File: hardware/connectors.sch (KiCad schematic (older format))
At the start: 16 parts, among them P1 Conn_01x12_Male, P10 Conn_01x12_Male, P11 Conn_01x12_Male, P12 Conn_01x12_Male, P13 Conn_01x12_Male, P14 Conn_01x12_Male, P15 Conn_01x12_Male, P16 Conn_01x12_Male, P2 Conn_01x12_Male, P3 Conn_01x12_Male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

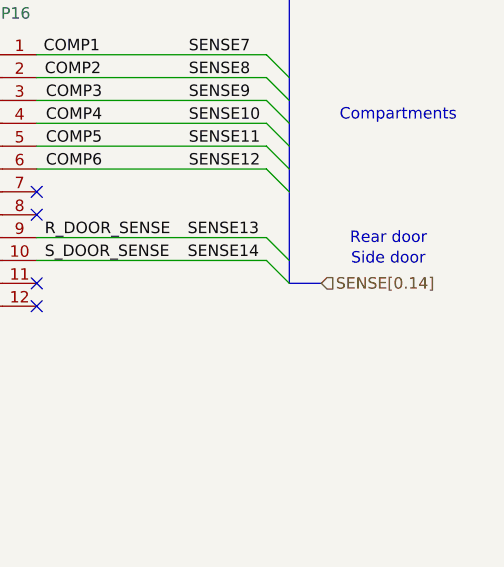
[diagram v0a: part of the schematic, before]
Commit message: hardware: fix mislabeled bus
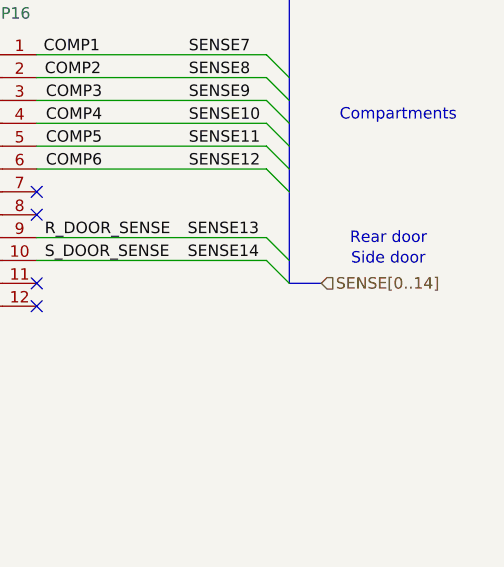
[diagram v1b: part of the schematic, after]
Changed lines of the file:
@@
 	14535 6650 14675 6650
 Text HLabel 14675 6650 2    50   Input ~ 0
-SENSE[0.14]
+SENSE[0..14]
 Wire Wire Line
 	13430 5950 14435 5950

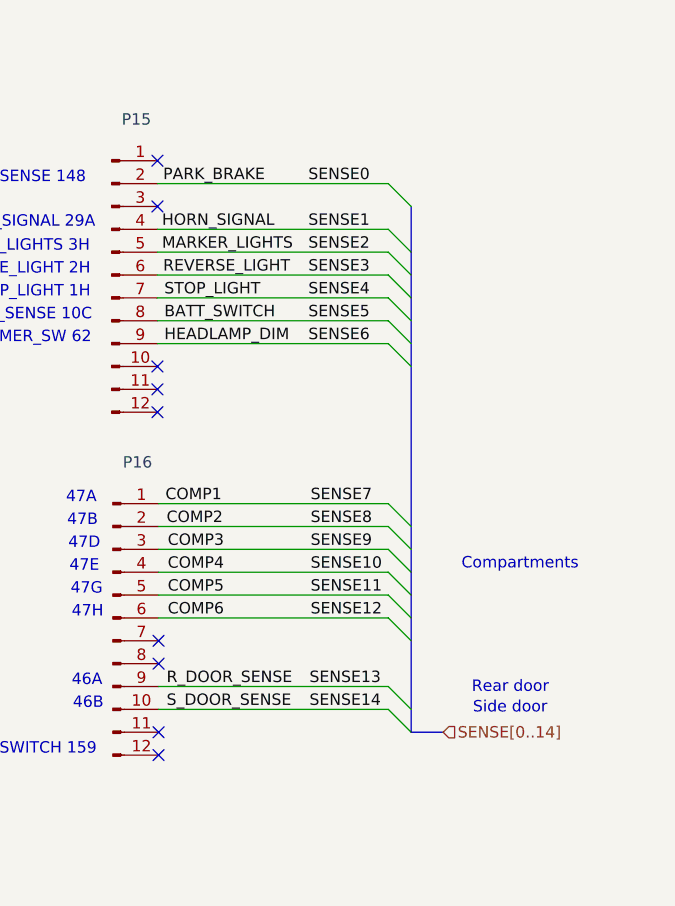
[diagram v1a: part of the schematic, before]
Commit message: hardware: split house and truck sense
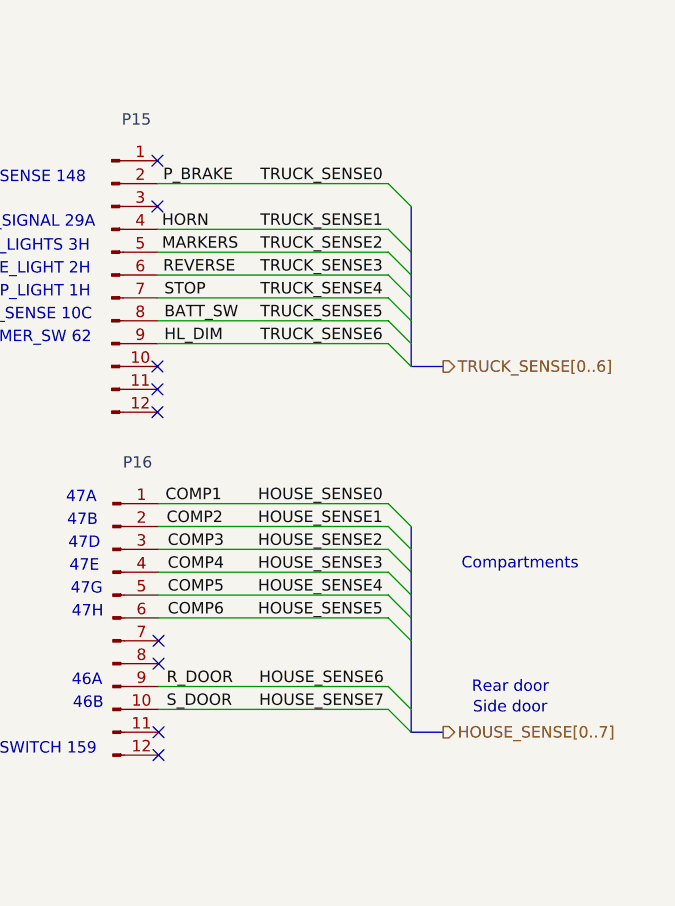
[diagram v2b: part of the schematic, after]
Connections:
- net BATT_SWITCH renamed BATT_SW
- net HEADLAMP_DIM renamed HL_DIM
- net HORN_SIGNAL renamed HORN
- net MARKER_LIGHTS renamed MARKERS
- net PARK_BRAKE renamed P_BRAKE
- net REVERSE_LIGHT renamed REVERSE
- net R_DOOR_SENSE renamed HOUSE_SENSE6
- net SENSE14 renamed HOUSE_SENSE7
- net SENSE4 renamed STOP
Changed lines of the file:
@@
 COMP6
 Text Label 13465 6450 0    50   ~ 0
-R_DOOR_SENSE
+R_DOOR
 Text Label 13465 6550 0    50   ~ 0
-S_DOOR_SENSE
-Text Label 14095 5650 0    50   ~ 0
-SENSE7
-Text Label 14095 5750 0    50   ~ 0
-SENSE8
-Text Label 14095 5850 0    50   ~ 0
-SENSE9
-Text Label 14095 5950 0    50   ~ 0
-SENSE10
-Text Label 14095 6050 0    50   ~ 0
-SENSE11
-Text Label 14095 6150 0    50   ~ 0
-SENSE12
-Text Label 14090 6450 0    50   ~ 0
-SENSE13
-Text Label 14090 6550 0    50   ~ 0
-SENSE14
+S_DOOR
+Text Label 13865 5650 0    50   ~ 0
+HOUSE_SENSE0
+Text Label 13865 5750 0    50   ~ 0
+HOUSE_SENSE1
+Text Label 13865 5850 0    50   ~ 0
+HOUSE_SENSE2
+Text Label 13865 5950 0    50   ~ 0
+HOUSE_SENSE3
+Text Label 13865 6050 0    50   ~ 0
+HOUSE_SENSE4
+Text Label 13865 6150 0    50   ~ 0
+HOUSE_SENSE5
+Text Label 13870 6450 0    50   ~ 0
+HOUSE_SENSE6
+Text Label 13870 6550 0    50   ~ 0
+HOUSE_SENSE7
 Text Label 13450 4250 0    50   ~ 0
-PARK_BRAKE
+P_BRAKE
 NoConn ~ 13425 4350
 Text Label 13445 4450 0    50   ~ 0
-HORN_SIGNAL
+HORN
 Text Label 13445 4550 0    50   ~ 0
-MARKER_LIGHTS
+MARKERS
 Text Label 13450 4650 0    50   ~ 0
-REVERSE_LIGHT
+REVERSE
 Text Label 13455 4750 0    50   ~ 0
-STOP_LIGHT
+STOP
 Text Label 13455 4850 0    50   ~ 0
-BATT_SWITCH
+BATT_SW
 Text Label 13455 4950 0    50   ~ 0
-HEADLAMP_DIM
-Text Label 14085 4950 0    50   ~ 0
-SENSE6
-Text Label 14085 4850 0    50   ~ 0
-SENSE5
-Text Label 14085 4750 0    50   ~ 0
-SENSE4
-Text Label 14085 4650 0    50   ~ 0
-SENSE3
-Text Label 14085 4550 0    50   ~ 0
-SENSE2
-Text Label 14085 4450 0    50   ~ 0
-SENSE1
-Text Label 14085 4250 0    50   ~ 0
-SENSE0
+HL_DIM
+Text Label 13875 4950 0    50   ~ 0
+TRUCK_SENSE6
+Text Label 13875 4850 0    50   ~ 0
+TRUCK_SENSE5
+Text Label 13875 4750 0    50   ~ 0
+TRUCK_SENSE4
+Text Label 13875 4650 0    50   ~ 0
+TRUCK_SENSE3
+Text Label 13875 4550 0    50   ~ 0
+TRUCK_SENSE2
+Text Label 13875 4450 0    50   ~ 0
+TRUCK_SENSE1
+Text Label 13875 4250 0    50   ~ 0
+TRUCK_SENSE0
 Entry Wire Line
 	14435 5650 14535 5750
@@
 Wire Bus Line
 	14535 6650 14675 6650
-Text HLabel 14675 6650 2    50   Input ~ 0
-SENSE[0..14]
+Text HLabel 14675 6650 2    50   Output ~ 0
+HOUSE_SENSE[0..7]
 Wire Wire Line
 	13430 5950 14435 5950
@@
 	8640 4985 9470 4985
 Wire Bus Line
-	14535 4350 14535 6650
+	14535 5050 14675 5050
+Text HLabel 14675 5050 2    50   Output ~ 0
+TRUCK_SENSE[0..6]
+Wire Bus Line
+	14535 5750 14535 6650
+Wire Bus Line
+	14535 4350 14535 5050
 $EndSCHEMATC
